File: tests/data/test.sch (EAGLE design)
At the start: 2 parts

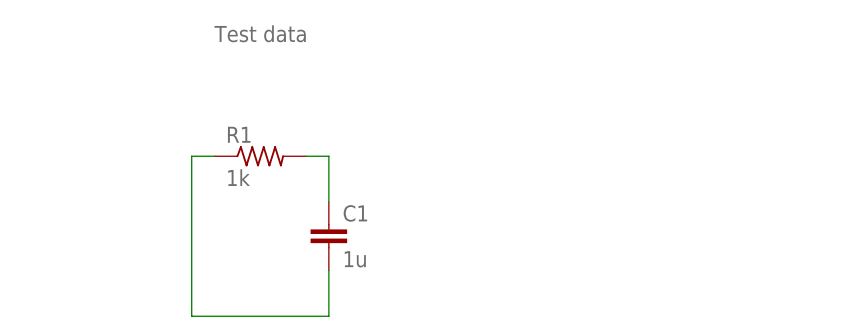
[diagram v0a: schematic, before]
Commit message: Support long pad (#17)
* Render long and offset pad
* Fix pad rotate
* Update test data
* Add rotated pad to test data
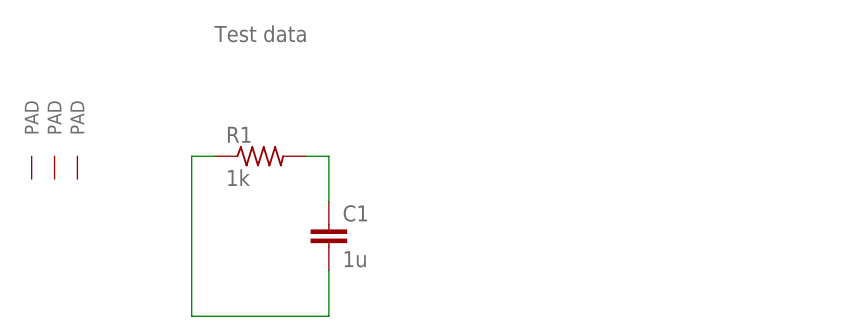
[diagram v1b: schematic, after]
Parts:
- added PAD1: PADLONG, pad:PADLONG
- added PAD2, PAD3: PADOFFSET, pad:PADOFFSET
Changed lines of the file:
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@@
 <part name="C1" library="rcl" deviceset="C-EU" device="C0402" value="1u"/>
 <part name="R1" library="rcl" deviceset="R-US_" device="R0402" value="1k"/>
+<part name="PAD1" library="pad" deviceset="PAD" device="LONG"/>
+<part name="PAD2" library="pad" deviceset="PAD" device="OFFSET"/>
+<part name="PAD3" library="pad" deviceset="PAD" device="OFFSET"/>
 </parts>
 <sheets>
@@
 <instance part="C1" gate="G$1" x="101.6" y="73.66"/>
 <instance part="R1" gate="G$1" x="93.98" y="81.28"/>
+<instance part="PAD1" gate="G" x="71.12" y="81.28" rot="R90"/>
+<instance part="PAD2" gate="G" x="68.58" y="81.28" rot="R90"/>
+<instance part="PAD3" gate="G" x="73.66" y="81.28" rot="R90"/>
 </instances>
 <busses>

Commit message: Fix text replace (#22)
* Add test for replacement

* Fix replace key
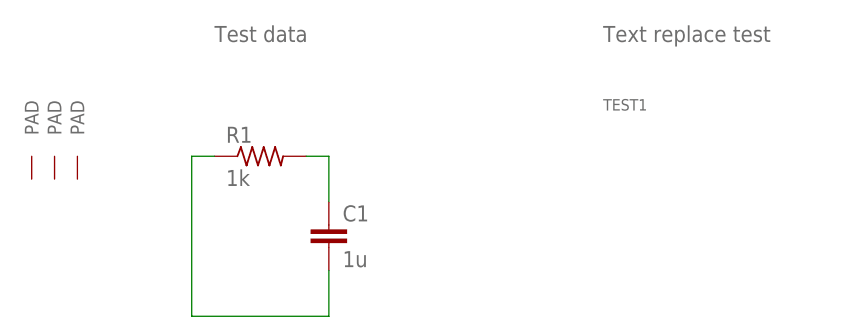
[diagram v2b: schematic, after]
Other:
- note added: "Text replace test"
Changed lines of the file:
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@@
 <part name="PAD2" library="pad" deviceset="PAD" device="OFFSET"/>
 <part name="PAD3" library="pad" deviceset="PAD" device="OFFSET"/>
+<part name="TEST1" library="pad" deviceset="REPLACE-TEST" device=""/>
 </parts>
 <sheets>
@@
 <plain>
 <text x="88.9" y="93.98" size="1.778" layer="95">Test data</text>
+<text x="132.08" y="93.98" size="1.778" layer="95">Text replace test</text>
 </plain>
 <instances>
@@
 <instance part="PAD2" gate="G" x="68.58" y="81.28" rot="R90"/>
 <instance part="PAD3" gate="G" x="73.66" y="81.28" rot="R90"/>
+<instance part="TEST1" gate="TEST" x="132.08" y="86.36"/>
 </instances>
 <busses>
